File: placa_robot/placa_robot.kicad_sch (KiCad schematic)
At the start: 1 part, among them IC1 MSP430FR2355TPT

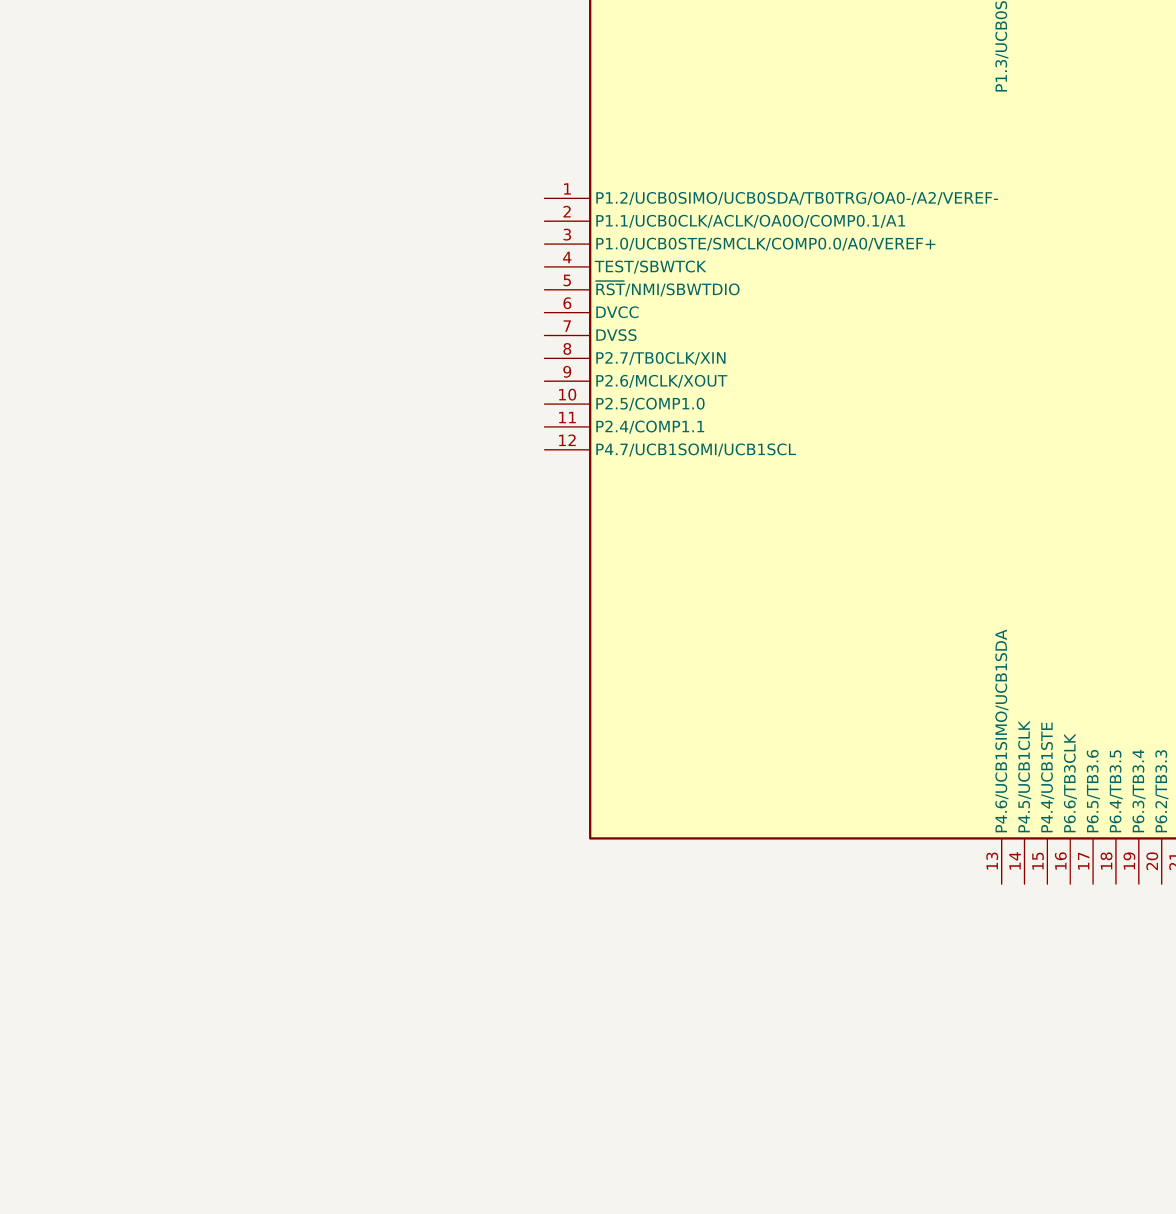
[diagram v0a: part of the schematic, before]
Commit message: I2C, Cuarzo, LCD
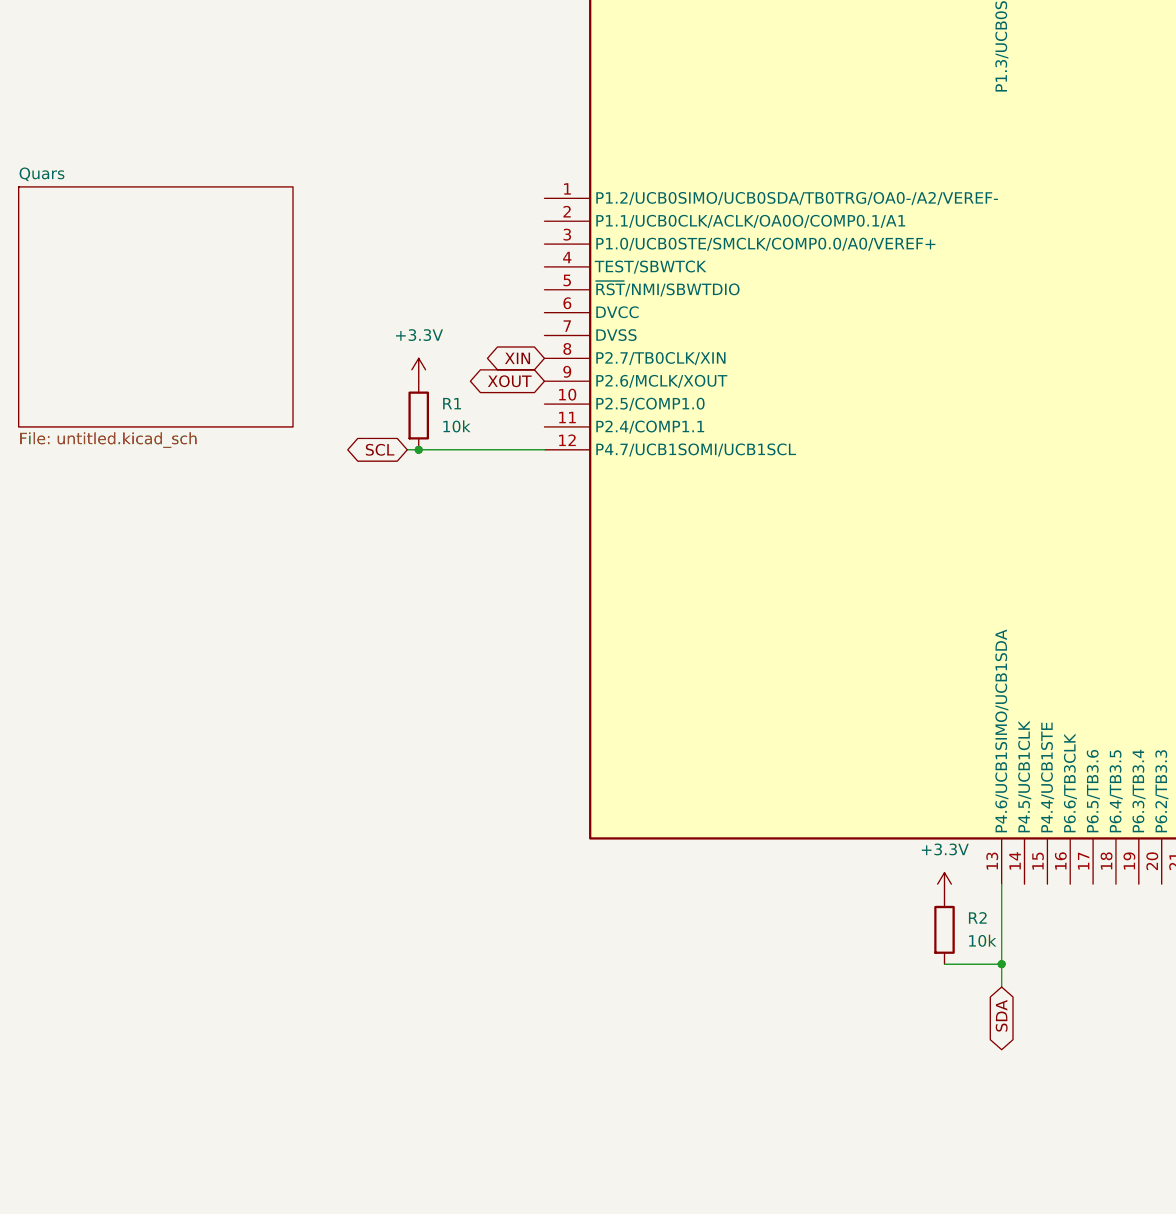
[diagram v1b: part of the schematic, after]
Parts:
- added R1, R2: 10k, symbol Device:R
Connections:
- net SCL: now reaches IC1.12 (P4.7/UCB1SOMI/UCB1SCL)
- net SCL: now also R1.2
- net SDA: now reaches IC1.13 (P4.6/UCB1SIMO/UCB1SDA)
- net SDA: now also R2.2
- net XIN: now reaches IC1.8 (P2.7/TB0CLK/XIN)
- net XOUT: now reaches IC1.9 (P2.6/MCLK/XOUT)
- new net +3.3V: R1.1, R2.1
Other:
- added sheet Quars (untitled.kicad_sch)

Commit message: Mas cosas
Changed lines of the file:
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@@
+	(wire
+		(pts
+			(xy 137.16 142.24) (xy 138.43 142.24)
+		)
+		(stroke
+			(width 0)
+			(type default)
+		)
+	)
 	(wire
 		(pts
@@
 	(global_label "XIN"
 		(shape bidirectional)
-		(at 138.43 142.24 180)
+		(at 137.16 142.24 180)
 		(fields_autoplaced yes)
 		(effects
@@
 		)
 		(property "Intersheetrefs" "${INTERSHEET_REFS}"
-			(at 131.1887 142.24 0)
+			(at 129.9187 142.24 0)
 			(effects
 				(font
